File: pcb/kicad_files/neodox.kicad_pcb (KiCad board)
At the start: 2 copper layers, 168.7 x 131.8 mm, 74 parts, among them K0 KEYSW, K1 KEYSW, K10 KEYSW, K11 KEYSW, K12 KEYSW, K13 KEYSW, K14 KEYSW, K15 KEYSW, K16 KEYSW, K2 KEYSW, K20 KEYSW, K21 KEYSW, K22 KEYSW, K23 KEYSW, K24 KEYSW, K25 KEYSW, K26 KEYSW, K3 KEYSW, K30 KEYSW, K31 KEYSW, K32 KEYSW, K33 KEYSW, K34 KEYSW, K35 KEYSW, K36 KEYSW, K4 KEYSW, K40 KEYSW, K41 KEYSW, K42 KEYSW, K43 KEYSW, K44 KEYSW, K45 KEYSW, K46 KEYSW, K5 KEYSW, K6 KEYSW, U1 ProMicro

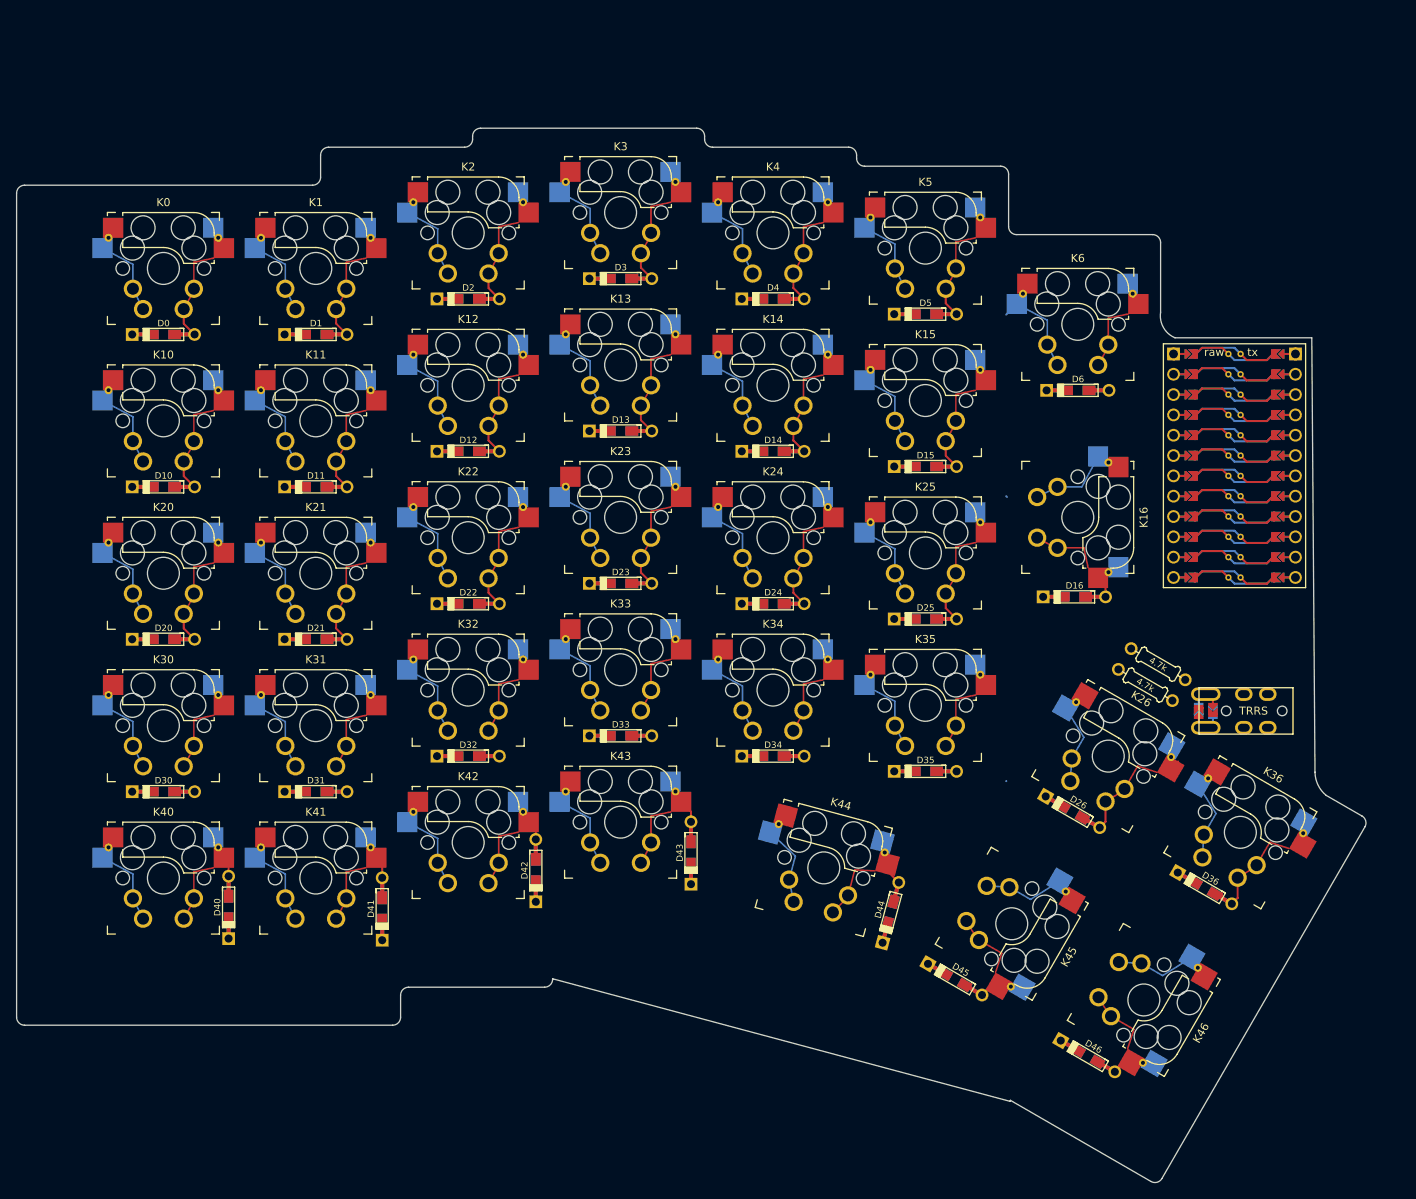
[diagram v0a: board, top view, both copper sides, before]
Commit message: add cutout
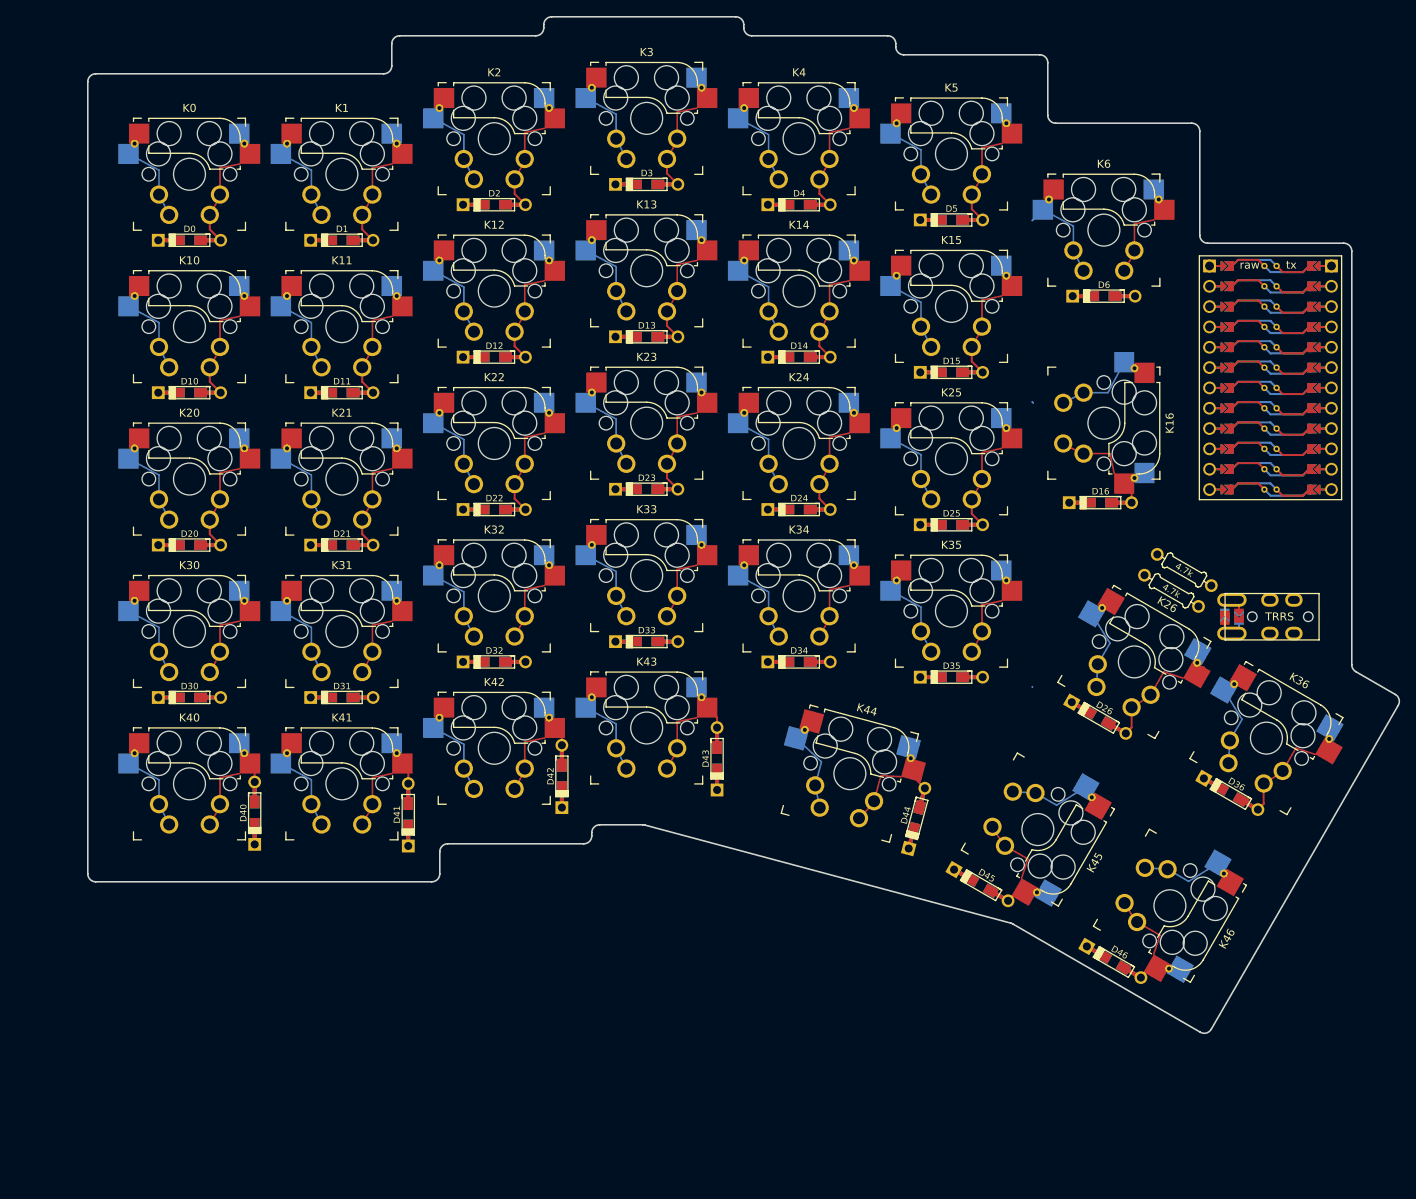
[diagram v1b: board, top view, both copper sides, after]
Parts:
- moved D13 12.2 mm to (123.3, 60.7)
- moved D16 12.2 mm to (180.0, 81.4)
- moved D23 12.2 mm to (123.3, 79.7)
- moved D24 12.2 mm to (142.3, 82.3)
- moved D26 12.2 mm to (179.8, 108.3)
- moved D34 12.2 mm to (142.3, 101.3)
- moved D35 12.2 mm to (161.4, 103.2)
- moved D40 12.2 mm to (74.3, 120.2)
- moved D43 12.2 mm to (132.1, 113.4)
- moved D44 12.2 mm to (157.0, 120.9)
- moved D45 12.2 mm to (165.1, 129.2)
- moved D46 12.2 mm to (181.7, 138.8)
- moved D6 12.2 mm to (180.4, 55.6)
- moved K16 12.2 mm to (180.4, 71.5)
- moved K23 12.2 mm to (123.3, 71.5)
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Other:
- board size 168.7 x 131.8 mm -> 163.9 x 127.1 mm
- board text removed: "raw"
- board text removed: "tx"
